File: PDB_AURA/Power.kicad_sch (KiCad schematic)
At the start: 17 parts, among them J100 XT30PW-M, Q100 CSD18540Q5B, U100 LM74700

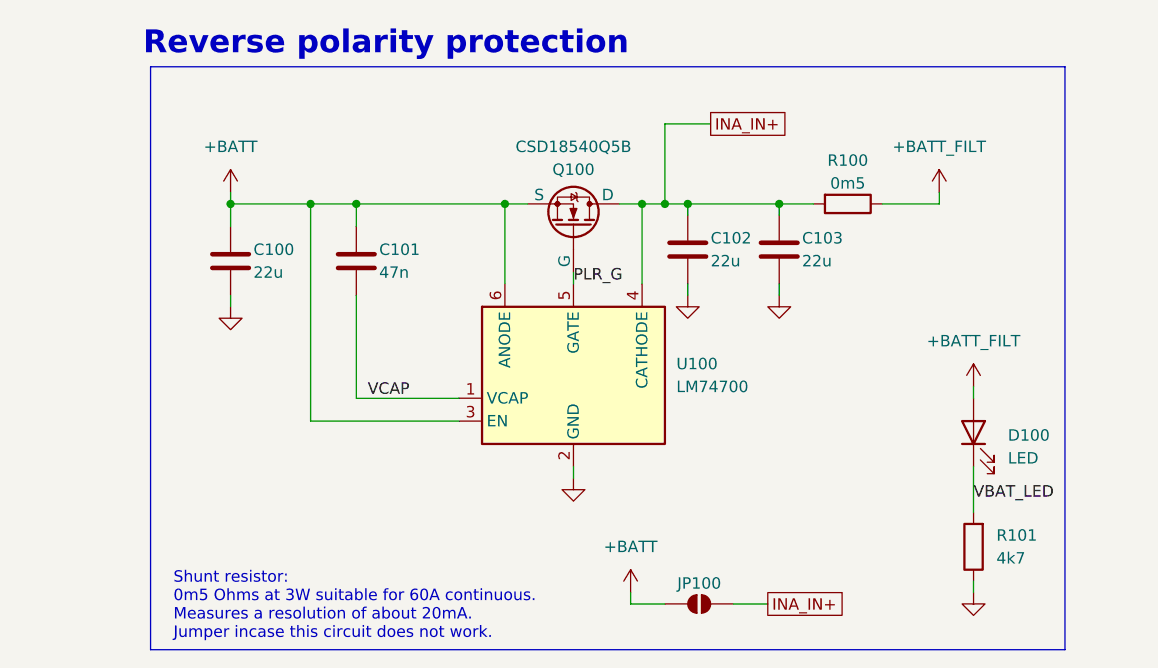
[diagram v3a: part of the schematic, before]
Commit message: Second Layout Attempt
Renamed all components and placed them all.
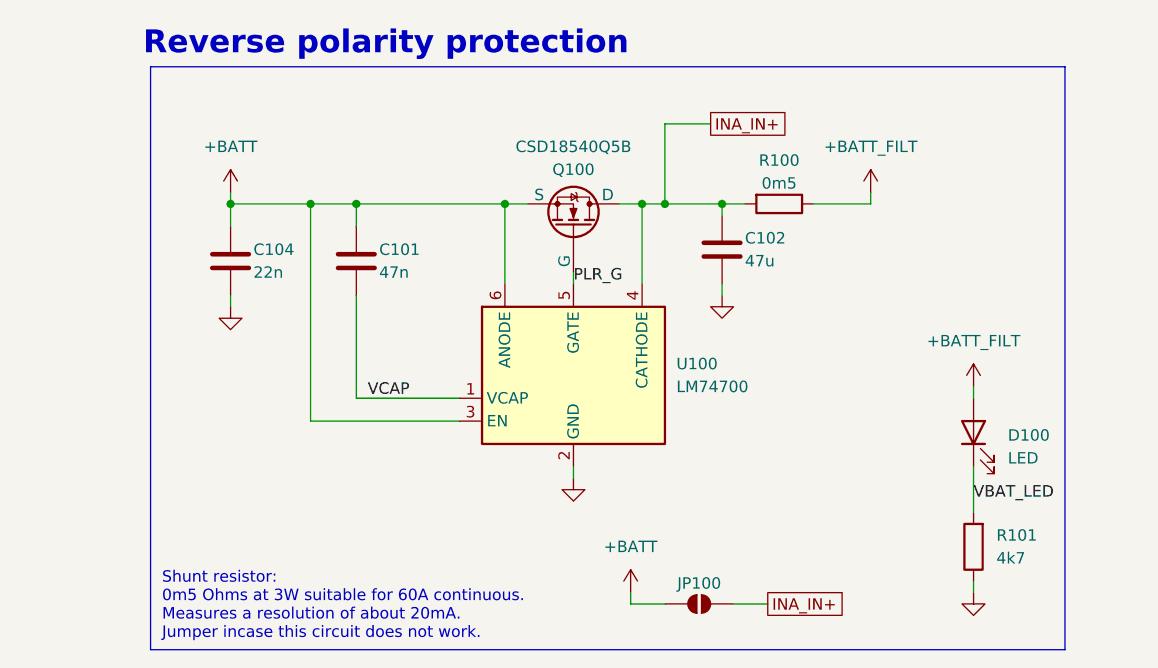
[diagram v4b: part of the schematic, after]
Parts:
- removed C100, C103: 22u, Capacitor_SMD:C_1210_3225Metric, symbol Device:C
- added C104: 22n, Capacitor_SMD:C_0402_1005Metric, symbol Device:C
- C102: value 22u -> 47u
- H100, H101, H102, H103: footprint MountingHole:MountingHole_4mm_Pad_Via -> MountingHole:MountingHole_3.2mm_M3_Pad_Via
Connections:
- net +BATT: now also C104.1
- net GND: now also C104.2
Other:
- moved on the sheet: C102, R100

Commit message: Started Routing
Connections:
- net +BATT: now also J100.4
- net GND: no longer J100.4
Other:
- note added: "Expected input 7V2 to 24V2. Pin 4 is +BATT to not interrupt copper pour."
- note removed: "Expected input 7V2 to 16V8"
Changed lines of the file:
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@@
 		)
 	)
-	(text "Expected input 7V2 to 16V8"
+	(text "Expected input 7V2 to 24V2.\nPin 4 is +BATT to not interrupt copper pour."
 		(exclude_from_sim no)
 		(at 36.83 105.41 0)
@@
 				(thickness 0.1588)
 			)
-			(justify left)
+			(justify left bottom)
 		)
 	)
@@
 	)
 	(junction
-		(at 74.93 88.9)
-		(diameter 0)
-		(color 0 0 0 0)
-	)
-	(junction
 		(at 50.8 86.36)
 		(diameter 0)
@@
 	(wire
 		(pts
-			(xy 74.93 88.9) (xy 74.93 97.79)
+			(xy 74.93 88.9) (xy 74.93 90.17)
 		)
 		(stroke
@@
 	(wire
 		(pts
-			(xy 74.93 86.36) (xy 74.93 88.9)
-		)
-		(stroke
-			(width 0)
-			(type default)
-		)
-	)
-	(wire
-		(pts
 			(xy 168.91 77.47) (xy 171.45 77.47)
 		)
@@
 		(pts
 			(xy 41.91 77.47) (xy 41.91 86.36)
+		)
+		(stroke
+			(width 0)
+			(type default)
+		)
+	)
+	(wire
+		(pts
+			(xy 74.93 86.36) (xy 74.93 83.82)
 		)
 		(stroke
@@
 				(justify left)
 				(hide yes)
+			)
+		)
+	)
+	(symbol
+		(lib_id "power:+BATT")
+		(at 74.93 83.82 0)
+		(unit 1)
+		(exclude_from_sim no)
+		(in_bom yes)
+		(on_board yes)
+		(dnp no)
+		(fields_autoplaced yes)
+		(property "Reference" "#PWR059"
+			(at 74.93 87.63 0)
+			(effects
+				(font
+					(size 1.27 1.27)
+				)
+				(hide yes)
+			)
+		)
+		(property "Value" "+BATT"
+			(at 74.93 78.74 0)
+			(effects
+				(font
+					(size 1.27 1.27)
+				)
+			)
+		)
+		(property "Footprint" ""
+			(at 74.93 83.82 0)
+			(effects
+				(font
+					(size 1.27 1.27)
+				)
+				(hide yes)
+			)
+		)
+		(property "Datasheet" ""
+			(at 74.93 83.82 0)
+			(effects
+				(font
+					(size 1.27 1.27)
+				)
+				(hide yes)
+			)
+		)
+		(property "Description" "Power symbol creates a global label with name \"+BATT\""
+			(at 74.93 83.82 0)
+			(effects
+				(font
+					(size 1.27 1.27)
+				)
+				(hide yes)
+			)
+		)
+		(pin "1"
+		)
+		(instances
+			(project "PDB_AURA"
+				(path "/c0b09de1-c640-438f-9ef5-dda14a6aac71/c5906580-2f17-4557-899f-eb3151fe9c9e"
+					(reference "#PWR059")
+					(unit 1)
+				)
 			)
 		)
@@
 	(symbol
 		(lib_id "power:GND")
-		(at 74.93 97.79 0)
+		(at 74.93 90.17 0)
 		(unit 1)
 		(exclude_from_sim no)
@@
 		(fields_autoplaced yes)
 		(property "Reference" "#PWR055"
-			(at 74.93 104.14 0)
+			(at 74.93 96.52 0)
 			(effects
 				(font
@@
 		)
 		(property "Value" "GND"
-			(at 74.93 102.87 0)
+			(at 74.93 95.25 0)
 			(effects
 				(font
@@
 		)
 		(property "Footprint" ""
-			(at 74.93 97.79 0)
+			(at 74.93 90.17 0)
 			(effects
 				(font
@@
 		)
 		(property "Datasheet" ""
-			(at 74.93 97.79 0)
+			(at 74.93 90.17 0)
 			(effects
 				(font
@@
 		)
 		(property "Description" "Power symbol creates a global label with name \"GND\" , ground"
-			(at 74.93 97.79 0)
-			(effects
-				(font
+			(at 74.93 90.17 0)
+			(effects
+				(font

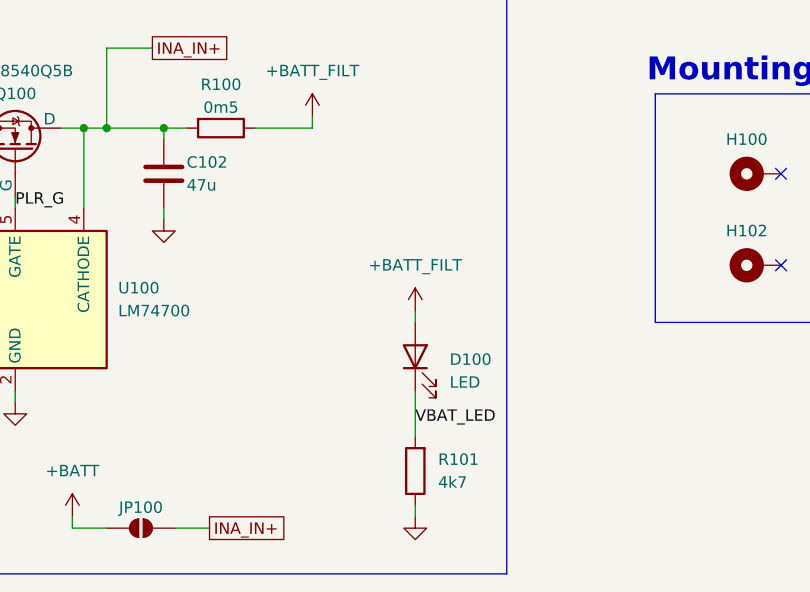
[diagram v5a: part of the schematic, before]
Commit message: New Component Values
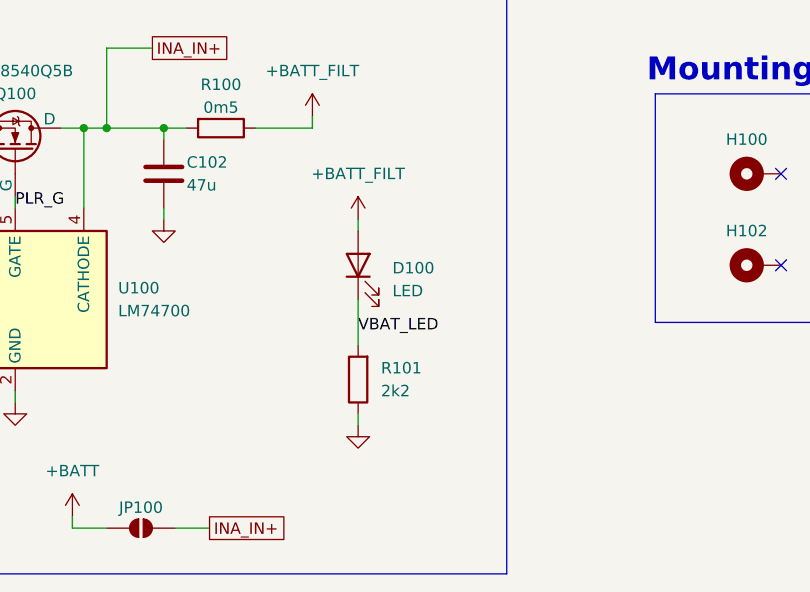
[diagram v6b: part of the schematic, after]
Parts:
- R101: value 4k7 -> 2k2
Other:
- moved on the sheet: D100, R101

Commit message: First review for PDB.
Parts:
- added TP100, TP101: TestPoint, TestPoint:TestPoint_Pad_D1.0mm, symbol Connector:TestPoint
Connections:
- net +BATT: now also TP100.1
- net +BATT_FILT: now also TP101.1

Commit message: Second iteration PDB
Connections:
- net GND: now also H100.1, H101.1, H102.1, H103.1
- no-connect marks 4 -> 0
